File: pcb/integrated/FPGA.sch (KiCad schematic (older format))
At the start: 27 parts, among them J3001 Conn_01x04_Male, J3002 Conn_01x06_Male, U3001 XC7S25-L1FTGB196, U3002 S25FL127SABN, U3003 74AVC4TD245BQ

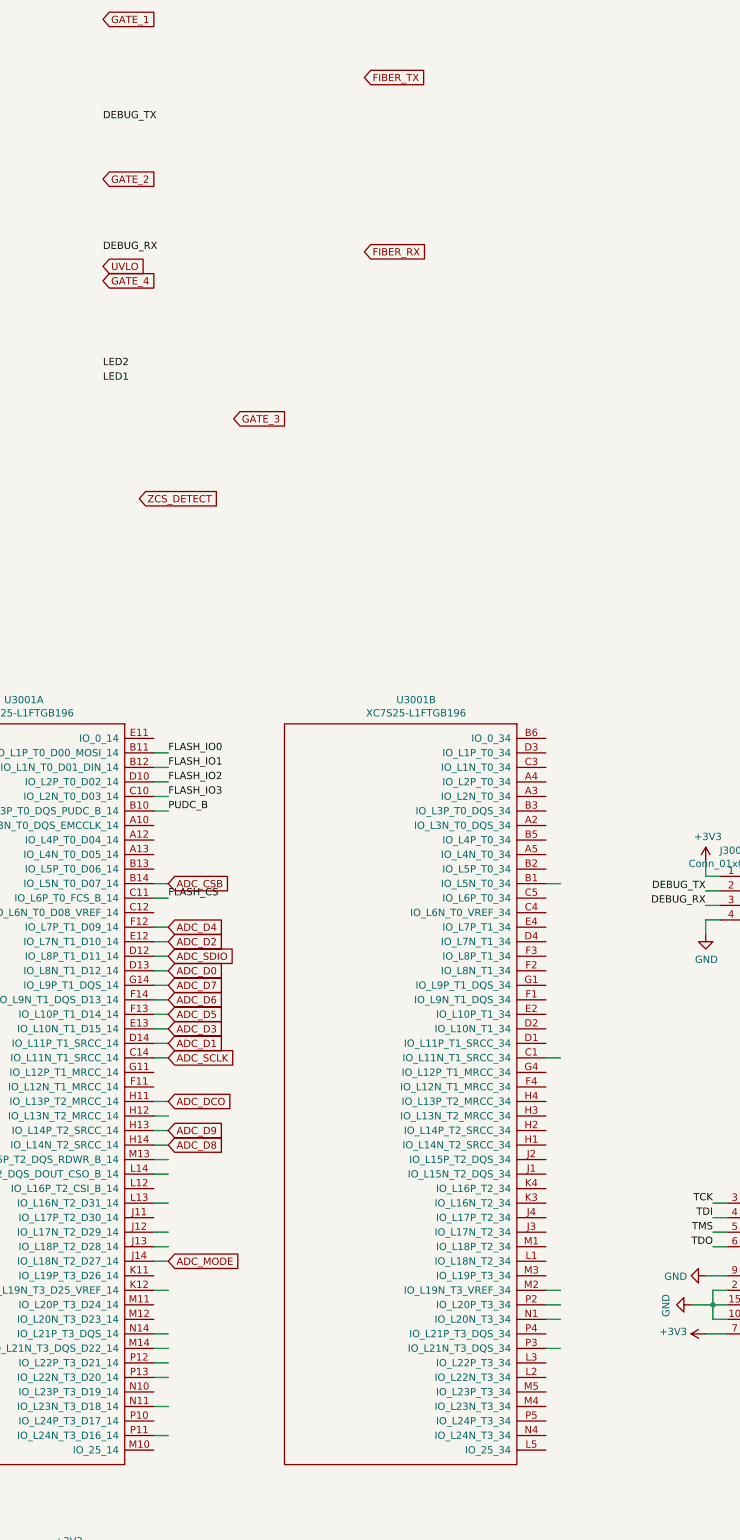
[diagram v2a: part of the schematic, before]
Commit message: redid power planes
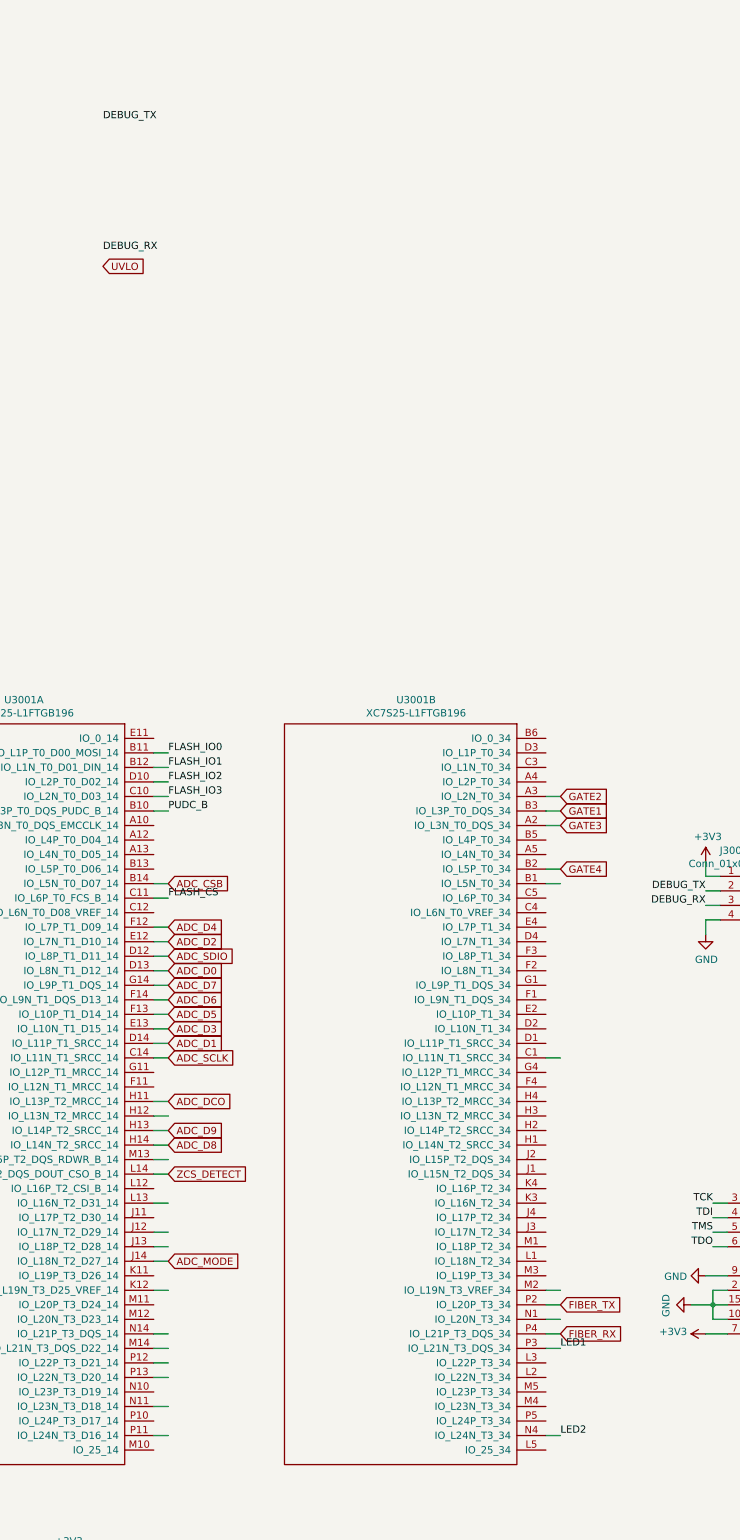
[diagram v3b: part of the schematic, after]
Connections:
- net labels added: GATE1, GATE2, GATE3, GATE4
- net labels removed: GATE_1, GATE_2, GATE_3, GATE_4
- wire segments 169 -> 175
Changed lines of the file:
@@
 Wire Wire Line
 	5300 1850 5400 1850
-Text GLabel 4950 -4100 2    50   Input ~ 0
-GATE_1
 Wire Wire Line
 	5300 2950 5400 2950
-Text GLabel 4950 -3000 2    50   Input ~ 0
-GATE_2
 Wire Wire Line
 	5300 2650 5400 2650
-Text GLabel 5850 -1350 2    50   Input ~ 0
-GATE_3
 Wire Wire Line
 	5300 3650 5400 3650
-Text GLabel 4950 -2300 2    50   Input ~ 0
-GATE_4
 Wire Wire Line
 	8000 4850 8100 4850
@@
 Wire Wire Line
 	8000 1850 8100 1850
-Text GLabel 6750 -3700 2    50   Input ~ 0
+Text GLabel 8100 4750 2    50   Input ~ 0
 FIBER_TX
-Text GLabel 6750 -2500 2    50   Input ~ 0
+Text GLabel 8100 4950 2    50   Input ~ 0
 FIBER_RX
 Wire Wire Line
@@
 Wire Wire Line
 	5300 3550 5400 3550
-Text GLabel 5200 -800 2    50   Input ~ 0
+Text GLabel 5400 3850 2    50   Input ~ 0
 ZCS_DETECT
 Wire Wire Line
@@
 Wire Wire Line
 	5300 4350 5400 4350
-Text Label 4950 -1600 0    50   ~ 0
+Text Label 8100 5050 0    50   ~ 0
 LED1
 Wire Wire Line
 	5300 4250 5400 4250
-Text Label 4950 -1700 0    50   ~ 0
+Text Label 8100 5650 0    50   ~ 0
 LED2
 $Comp
@@
 Wire Wire Line
 	5300 3050 5400 3050
+Wire Wire Line
+	8000 1750 8100 1750
+Text GLabel 8100 1750 2    50   Input ~ 0
+GATE4
+Wire Wire Line
+	8000 1450 8100 1450
+Text GLabel 8100 1450 2    50   Input ~ 0
+GATE3
+Wire Wire Line
+	8000 1350 8100 1350
+Text GLabel 8100 1350 2    50   Input ~ 0
+GATE1
+Wire Wire Line
+	8000 1250 8100 1250
+Text GLabel 8100 1250 2    50   Input ~ 0
+GATE2
+Wire Wire Line
+	8000 5650 8100 5650
+Wire Wire Line
+	8000 4950 8100 4950
 $EndSCHEMATC

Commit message: PCB routing finihsed, ready for design review
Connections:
- net labels added: BOOST_SW, CHARGE_SW
- wire segments 175 -> 177
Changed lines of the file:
@@
 Wire Wire Line
 	5300 3450 5400 3450
-Text Label 4950 -2500 0    50   ~ 0
+Text Label 5400 5050 0    50   ~ 0
 DEBUG_RX
 Wire Wire Line
 	5300 2550 5400 2550
-Text Label 4950 -3400 0    50   ~ 0
+Text Label 5400 4950 0    50   ~ 0
 DEBUG_TX
 Wire Wire Line
@@
 Wire Wire Line
 	8000 4950 8100 4950
+Text GLabel 8100 1150 2    50   Input ~ 0
+BOOST_SW
+Wire Wire Line
+	8000 1150 8100 1150
+Wire Wire Line
+	8000 1650 8100 1650
+Text GLabel 8100 1650 2    50   Input ~ 0
+CHARGE_SW
 $EndSCHEMATC

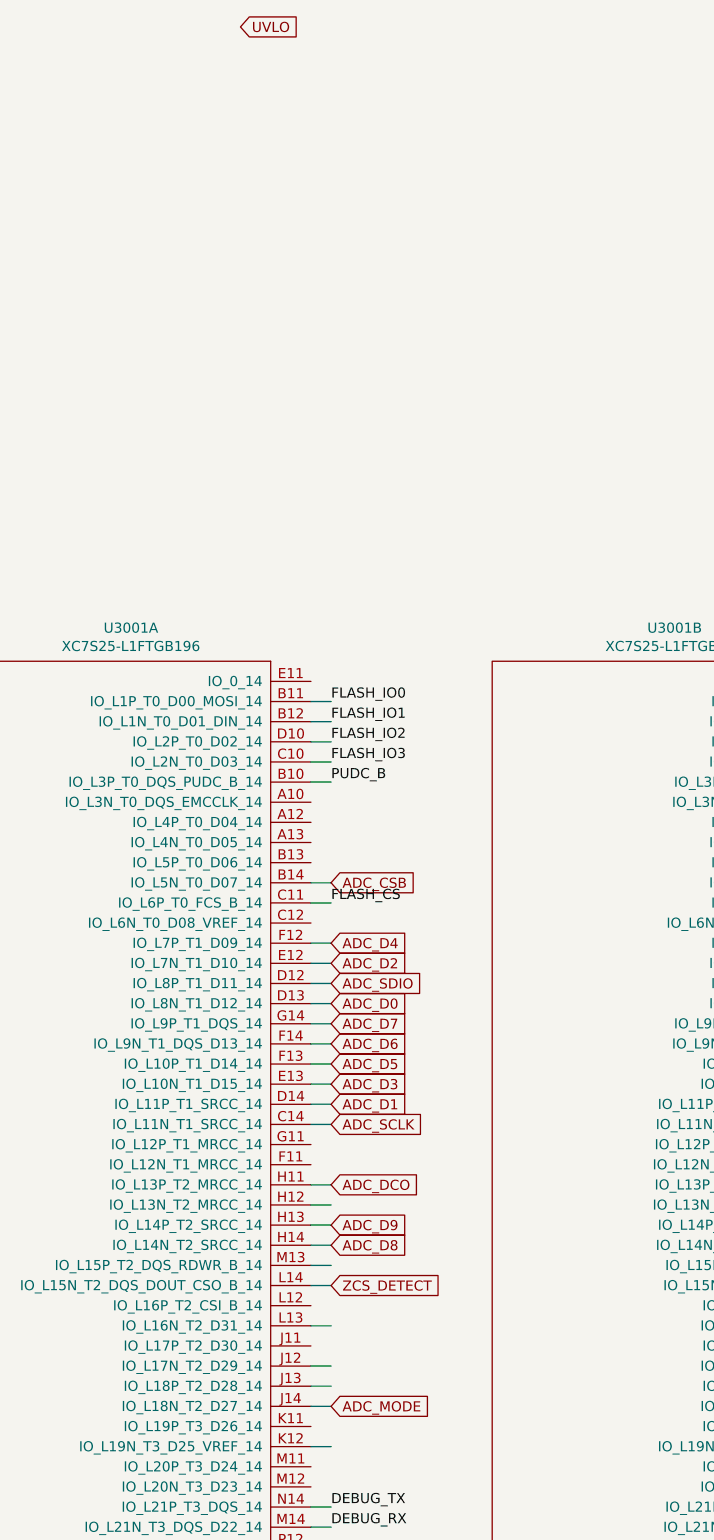
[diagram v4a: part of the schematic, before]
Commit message: finished design review and sent PCB to fab
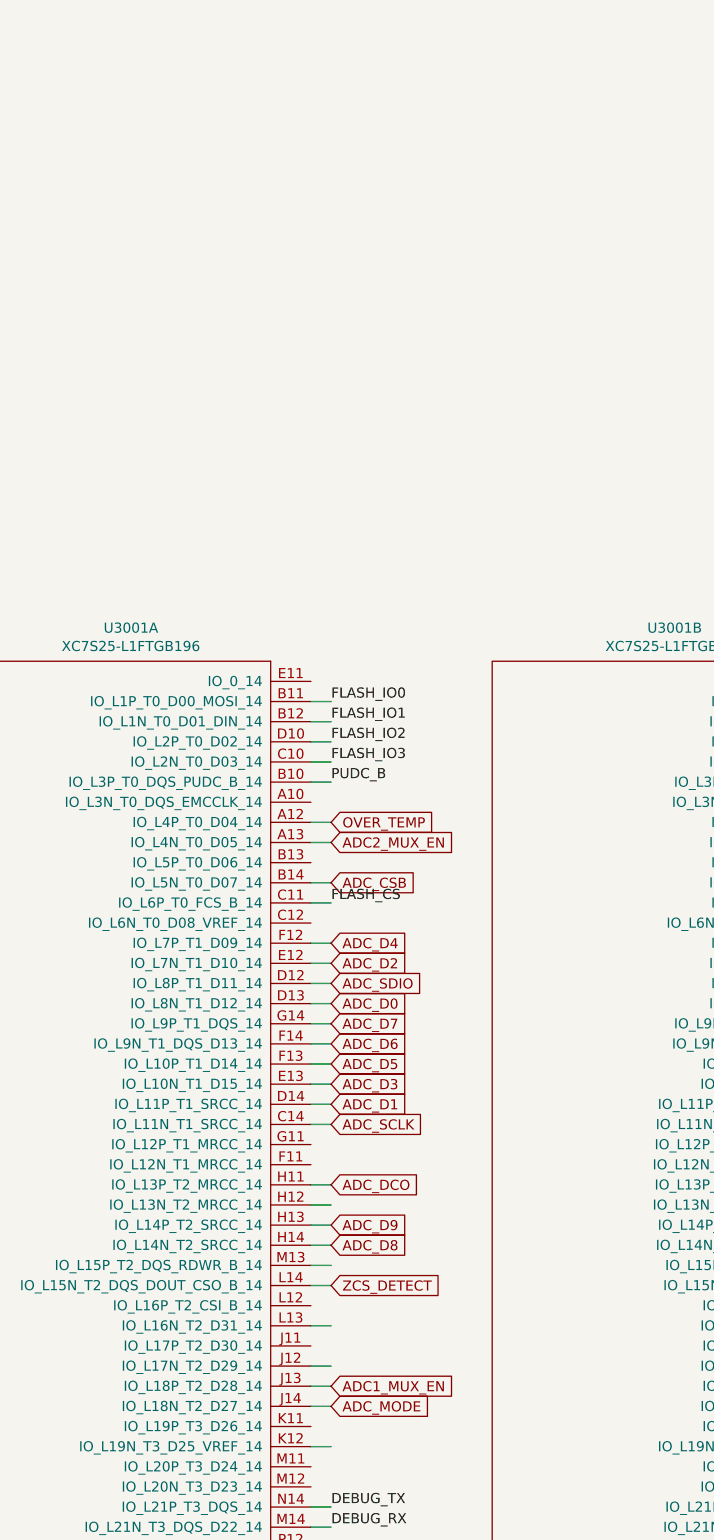
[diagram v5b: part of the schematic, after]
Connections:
- net labels added: ADC1_MUX_EN, ADC2_MUX_EN, OVER_TEMP
- net labels removed: UVLO
- wire segments 177 -> 179
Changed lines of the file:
@@
 Wire Wire Line
 	5300 4650 5400 4650
-Text GLabel 4950 -2400 2    50   Input ~ 0
-UVLO
 Wire Wire Line
 	5300 3450 5400 3450
@@
 Text GLabel 8100 1650 2    50   Input ~ 0
 CHARGE_SW
+Text GLabel 5400 4350 2    50   Input ~ 0
+ADC1_MUX_EN
+Wire Wire Line
+	5300 1650 5400 1650
+Text GLabel 5400 1650 2    50   Input ~ 0
+ADC2_MUX_EN
+Text GLabel 5400 1550 2    50   Input ~ 0
+OVER_TEMP
+Wire Wire Line
+	5300 1550 5400 1550
 $EndSCHEMATC

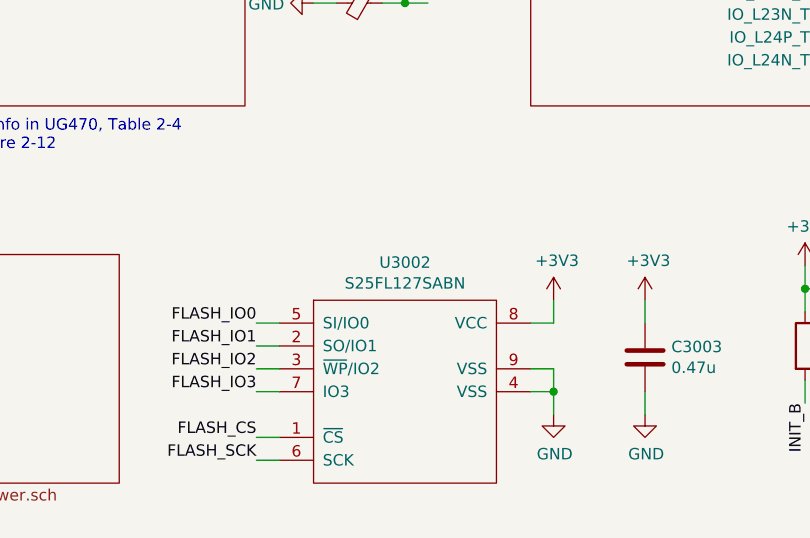
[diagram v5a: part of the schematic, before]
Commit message: updated component values for schematic
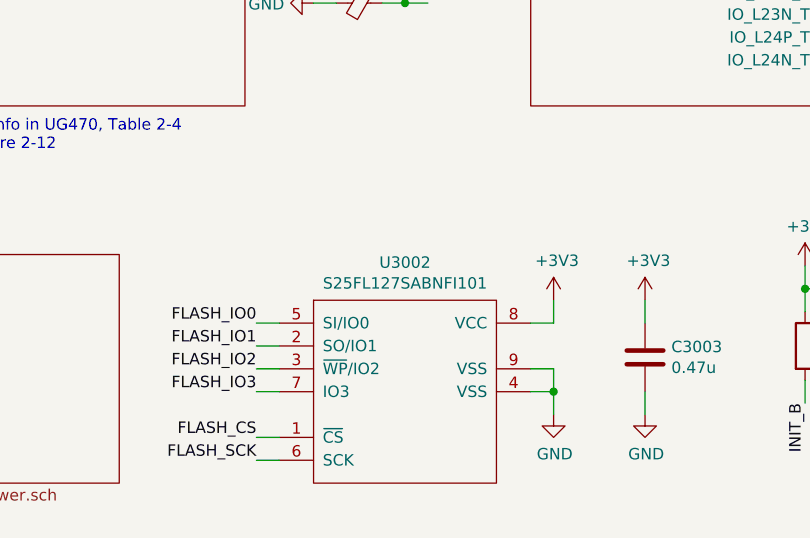
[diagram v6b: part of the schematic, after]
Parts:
- U3002: value S25FL127SABN -> S25FL127SABNFI101
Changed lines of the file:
@@
 EESchema Schematic File Version 4
 LIBS:integrated-cache
-EELAYER 30 0
+EELAYER 26 0
 EELAYER END
 $Descr A4 11693 8268
@@
 P 2950 7100
 F 0 "U3002" H 2950 7665 50  0000 C CNN
-F 1 "S25FL127SABN" H 2950 7574 50  0000 C CNN
+F 1 "S25FL127SABNFI101" H 2950 7574 50  0000 C CNN
 F 2 "wbraun_smd:WSON-8-1EP_6x5mm_P1.27mm_EP3.4x4mm" H 3150 7450 50  0001 C CNN
 F 3 "" H 3150 7450 50  0001 C CNN
